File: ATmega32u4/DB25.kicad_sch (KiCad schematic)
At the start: 3 parts, among them J4 DB25_Male_MountingHoles

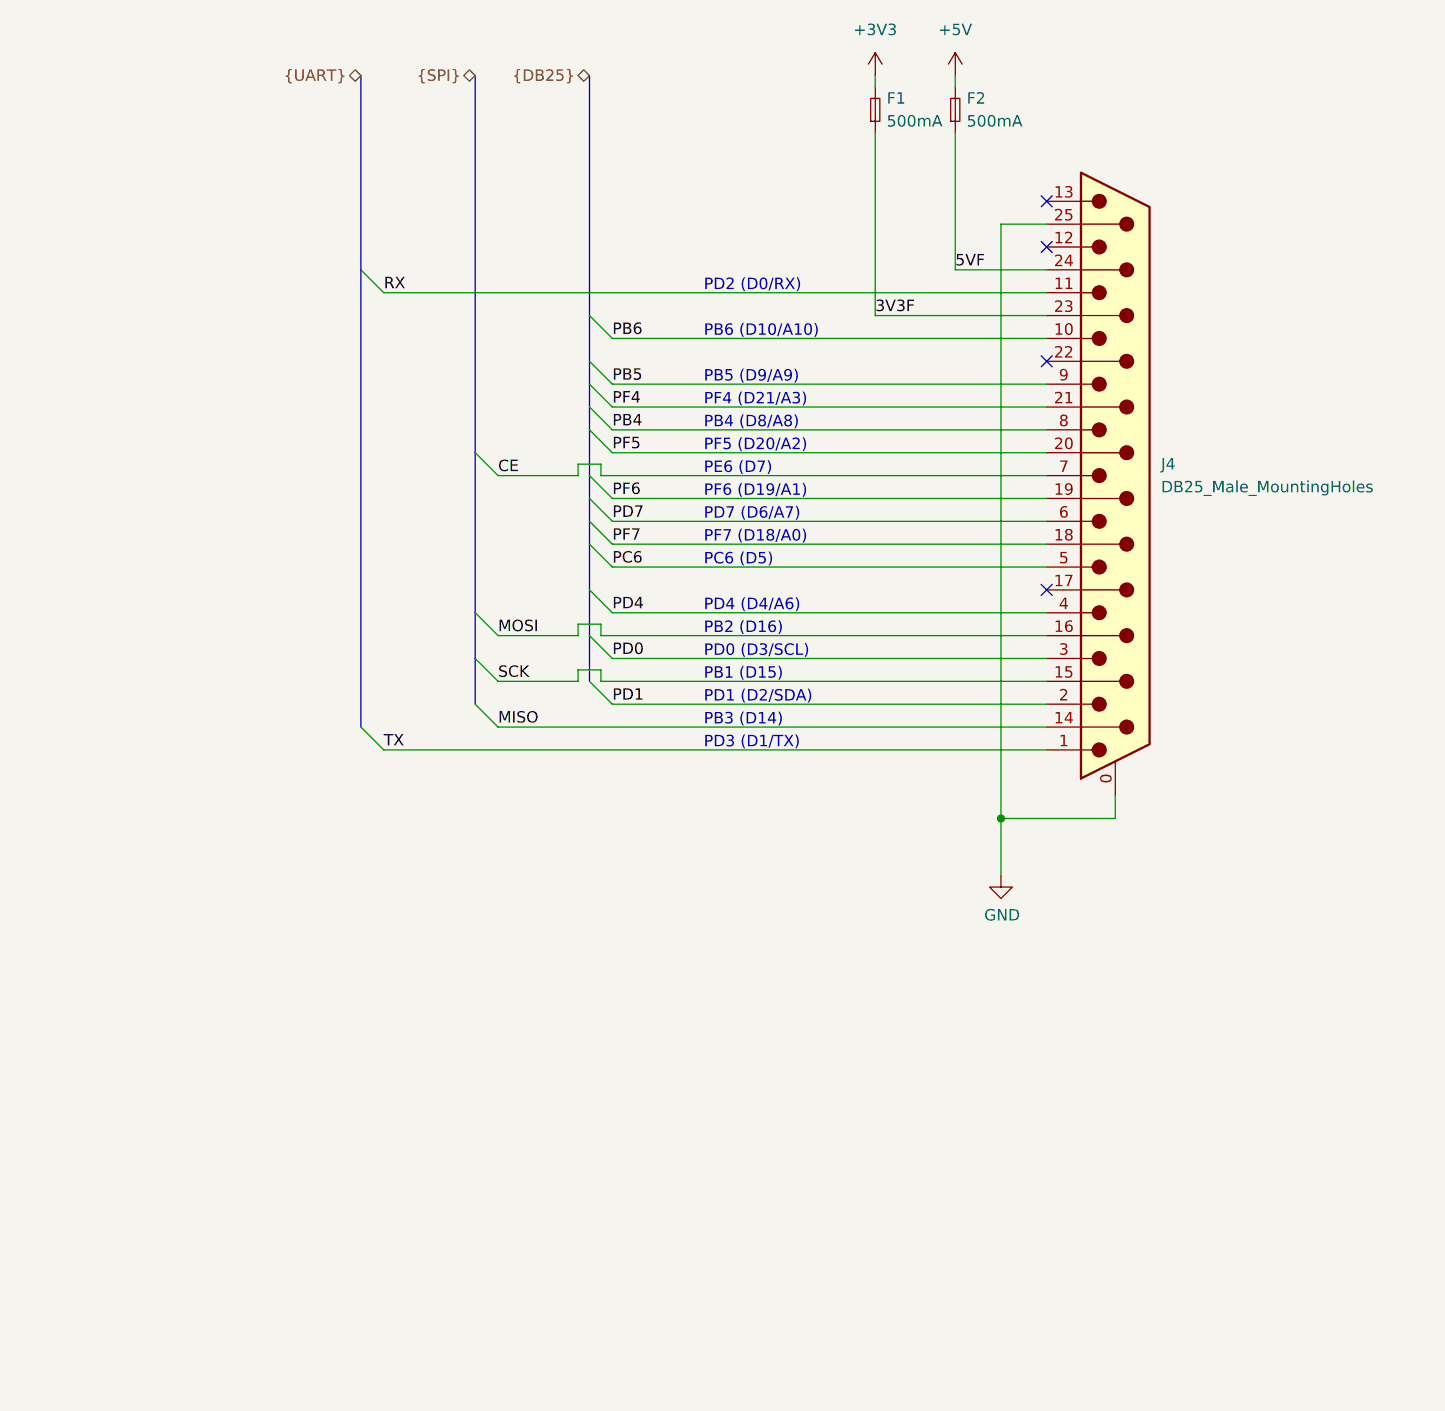
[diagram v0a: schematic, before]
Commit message: Schematic, routing and layout changes post review.
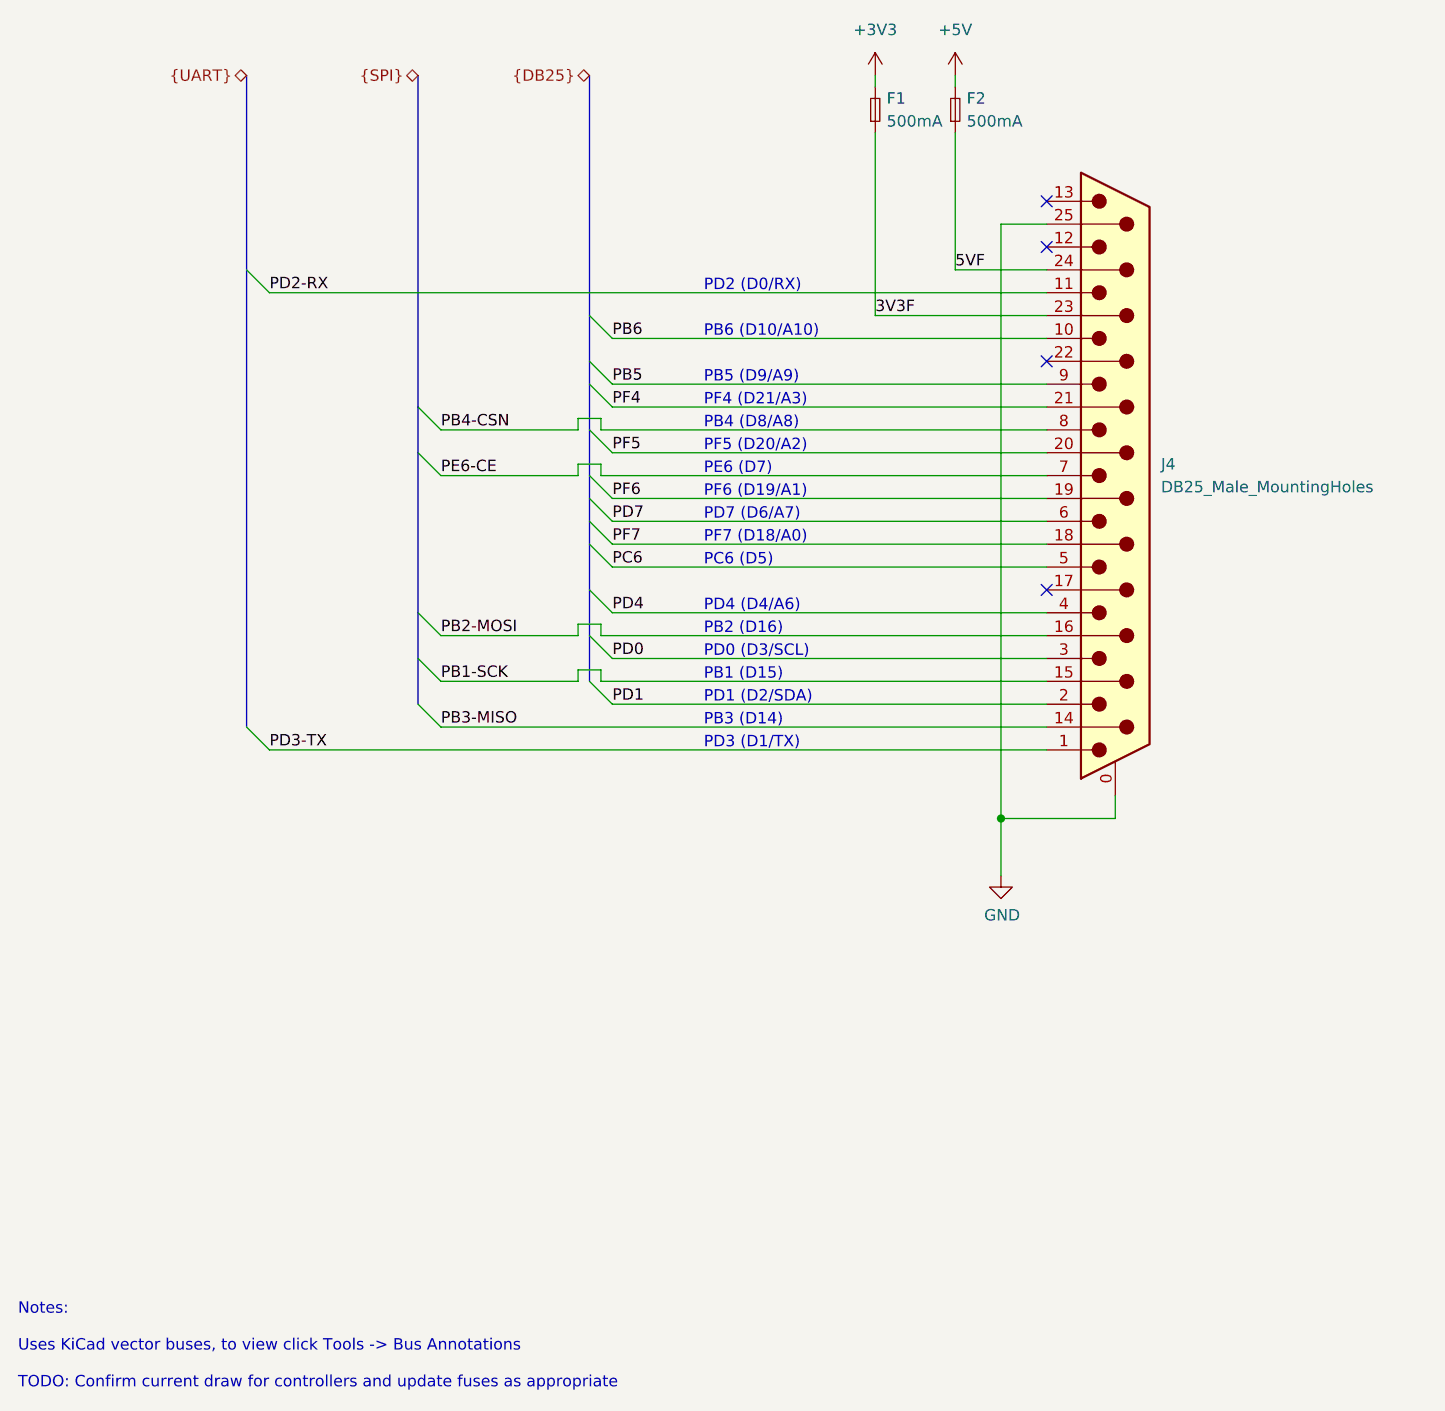
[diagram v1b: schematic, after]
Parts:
- J4: now in the parts list
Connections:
- net CE renamed PE6-CE
- net MISO renamed PB3-MISO
- net MOSI renamed PB2-MOSI
- net PB4 renamed PB4-CSN
- net RX renamed PD2-RX
- net SCK renamed PB1-SCK
- net TX renamed PD3-TX
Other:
- note added: "Notes: Uses KiCad vector buses, to view click Tools -> Bus Annotations TODO: Confirm current draw for controllers and update fuses as appropriate"
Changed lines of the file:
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@@
   (no_connect (at 127 82.55))
   (no_connect (at 127 64.77))
-  (bus_entry (at 63.5 115.57) (size 2.54 2.54)
+  (bus_entry (at 57.15 115.57) (size 2.54 2.54)
     (stroke (width 0) (type default) (color 0 0 0 0))
   )
@@
     (stroke (width 0) (type default) (color 0 0 0 0))
   )
-  (bus_entry (at 63.5 120.65) (size 2.54 2.54)
+  (bus_entry (at 57.15 120.65) (size 2.54 2.54)
     (stroke (width 0) (type default) (color 0 0 0 0))
   )
@@
     (stroke (width 0) (type default) (color 0 0 0 0))
   )
+  (bus_entry (at 57.15 87.63) (size 2.54 2.54)
+    (stroke (width 0) (type default) (color 0 0 0 0))
+  )
   (bus_entry (at 76.2 85.09) (size 2.54 2.54)
     (stroke (width 0) (type default) (color 0 0 0 0))
@@
     (stroke (width 0) (type default) (color 0 0 0 0))
   )
-  (bus_entry (at 63.5 110.49) (size 2.54 2.54)
-    (stroke (width 0) (type default) (color 0 0 0 0))
-  )
-  (bus_entry (at 76.2 87.63) (size 2.54 2.54)
+  (bus_entry (at 57.15 110.49) (size 2.54 2.54)
     (stroke (width 0) (type default) (color 0 0 0 0))
   )
@@
     (stroke (width 0) (type default) (color 0 0 0 0))
   )
-  (bus_entry (at 50.8 72.39) (size 2.54 2.54)
-    (stroke (width 0) (type default) (color 0 0 0 0))
-  )
-  (bus_entry (at 63.5 92.71) (size 2.54 2.54)
+  (bus_entry (at 38.1 72.39) (size 2.54 2.54)
+    (stroke (width 0) (type default) (color 0 0 0 0))
+  )
+  (bus_entry (at 57.15 92.71) (size 2.54 2.54)
     (stroke (width 0) (type default) (color 0 0 0 0))
   )
@@
     (stroke (width 0) (type default) (color 0 0 0 0))
   )
-  (bus_entry (at 50.8 123.19) (size 2.54 2.54)
+  (bus_entry (at 38.1 123.19) (size 2.54 2.54)
     (stroke (width 0) (type default) (color 0 0 0 0))
   )
@@
     (stroke (width 0) (type default) (color 0 0 0 0))
   )
-  (bus (pts (xy 63.5 92.71) (xy 63.5 110.49))
+  (bus (pts (xy 57.15 92.71) (xy 57.15 110.49))
     (stroke (width 0) (type default) (color 0 0 0 0))
   )
@@
     (stroke (width 0) (type default) (color 0 0 0 0))
   )
-  (wire (pts (xy 66.04 118.11) (xy 74.93 118.11))
+  (wire (pts (xy 59.69 118.11) (xy 74.93 118.11))
     (stroke (width 0) (type default) (color 0 0 0 0))
   )
@@
     (stroke (width 0) (type default) (color 0 0 0 0))
   )
-  (wire (pts (xy 66.04 113.03) (xy 74.93 113.03))
+  (wire (pts (xy 59.69 113.03) (xy 74.93 113.03))
     (stroke (width 0) (type default) (color 0 0 0 0))
   )
@@
     (stroke (width 0) (type default) (color 0 0 0 0))
   )
-  (wire (pts (xy 53.34 74.93) (xy 127 74.93))
+  (wire (pts (xy 40.64 74.93) (xy 127 74.93))
     (stroke (width 0) (type default) (color 0 0 0 0))
   )
@@
     (stroke (width 0) (type default) (color 0 0 0 0))
   )
-  (bus (pts (xy 76.2 85.09) (xy 76.2 87.63))
+  (wire (pts (xy 77.47 88.9) (xy 74.93 88.9))
+    (stroke (width 0) (type default) (color 0 0 0 0))
+  )
+  (bus (pts (xy 76.2 85.09) (xy 76.2 90.17))
     (stroke (width 0) (type default) (color 0 0 0 0))
   )
@@
     (stroke (width 0) (type default) (color 0 0 0 0))
   )
-  (bus (pts (xy 63.5 115.57) (xy 63.5 120.65))
+  (bus (pts (xy 57.15 115.57) (xy 57.15 120.65))
     (stroke (width 0) (type default) (color 0 0 0 0))
   )
@@
     (stroke (width 0) (type default) (color 0 0 0 0))
   )
-  (bus (pts (xy 50.8 50.8) (xy 50.8 72.39))
+  (bus (pts (xy 38.1 50.8) (xy 38.1 72.39))
     (stroke (width 0) (type default) (color 0 0 0 0))
   )
@@
     (stroke (width 0) (type default) (color 0 0 0 0))
   )
+  (bus (pts (xy 57.15 87.63) (xy 57.15 92.71))
+    (stroke (width 0) (type default) (color 0 0 0 0))
+  )
   (wire (pts (xy 78.74 92.71) (xy 127 92.71))
     (stroke (width 0) (type default) (color 0 0 0 0))
@@
     (stroke (width 0) (type default) (color 0 0 0 0))
   )
+  (wire (pts (xy 77.47 90.17) (xy 77.47 88.9))
+    (stroke (width 0) (type default) (color 0 0 0 0))
+  )
   (wire (pts (xy 78.74 120.65) (xy 127 120.65))
     (stroke (width 0) (type default) (color 0 0 0 0))
   )
-  (wire (pts (xy 78.74 90.17) (xy 127 90.17))
-    (stroke (width 0) (type default) (color 0 0 0 0))
-  )
-  (wire (pts (xy 53.34 125.73) (xy 127 125.73))
+  (wire (pts (xy 40.64 125.73) (xy 127 125.73))
     (stroke (width 0) (type default) (color 0 0 0 0))
   )
@@
     (stroke (width 0) (type default) (color 0 0 0 0))
   )
-  (bus (pts (xy 50.8 72.39) (xy 50.8 123.19))
+  (bus (pts (xy 38.1 72.39) (xy 38.1 123.19))
     (stroke (width 0) (type default) (color 0 0 0 0))
   )
@@
     (stroke (width 0) (type default) (color 0 0 0 0))
   )
+  (wire (pts (xy 77.47 90.17) (xy 127 90.17))
+    (stroke (width 0) (type default) (color 0 0 0 0))
+  )
   (wire (pts (xy 78.74 80.01) (xy 127 80.01))
     (stroke (width 0) (type default) (color 0 0 0 0))
@@
     (stroke (width 0) (type default) (color 0 0 0 0))
   )
-  (bus (pts (xy 63.5 110.49) (xy 63.5 115.57))
+  (wire (pts (xy 59.69 90.17) (xy 74.93 90.17))
+    (stroke (width 0) (type default) (color 0 0 0 0))
+  )
+  (wire (pts (xy 74.93 88.9) (xy 74.93 90.17))
+    (stroke (width 0) (type default) (color 0 0 0 0))
+  )
+  (bus (pts (xy 57.15 110.49) (xy 57.15 115.57))
     (stroke (width 0) (type default) (color 0 0 0 0))
   )
@@
     (stroke (width 0) (type default) (color 0 0 0 0))
   )
-  (wire (pts (xy 66.04 95.25) (xy 74.93 95.25))
+  (wire (pts (xy 59.69 95.25) (xy 74.93 95.25))
     (stroke (width 0) (type default) (color 0 0 0 0))
   )
@@
     (stroke (width 0) (type default) (color 0 0 0 0))
   )
-  (bus (pts (xy 76.2 87.63) (xy 76.2 90.17))
-    (stroke (width 0) (type default) (color 0 0 0 0))
-  )
-  (bus (pts (xy 63.5 50.8) (xy 63.5 92.71))
-    (stroke (width 0) (type default) (color 0 0 0 0))
-  )
-  (wire (pts (xy 66.04 123.19) (xy 127 123.19))
-    (stroke (width 0) (type default) (color 0 0 0 0))
+  (bus (pts (xy 57.15 50.8) (xy 57.15 87.63))
+    (stroke (width 0) (type default) (color 0 0 0 0))
+  )
+  (wire (pts (xy 59.69 123.19) (xy 127 123.19))
+    (stroke (width 0) (type default) (color 0 0 0 0))
+  )
+  (text "Notes:\n\nUses KiCad vector buses, to view click Tools -> Bus Annotations\n\nTODO: Confirm current draw for controllers and update fuses as appropriate"
+    (at 12.7 196.85 0)
+    (effects (font (size 1.27 1.27)) (justify left bottom))
   )
   (text "PD2 (D0/RX)" (at 88.9 74.93 0)
@@
     (effects (font (size 1.27 1.27)) (justify left bottom))
   )
-  (label "PB4" (at 78.74 90.17 0)
-    (effects (font (size 1.27 1.27)) (justify left bottom))
-  )
   (label "PB5" (at 78.74 85.09 0)
     (effects (font (size 1.27 1.27)) (justify left bottom))
   )
-  (label "MOSI" (at 66.04 113.03 0)
+  (label "PB2-MOSI" (at 59.69 113.03 0)
     (effects (font (size 1.27 1.27)) (justify left bottom))
   )
@@
     (effects (font (size 1.27 1.27)) (justify left bottom))
   )
-  (label "MISO" (at 66.04 123.19 0)
-    (effects (font (size 1.27 1.27)) (justify left bottom))
-  )
-  (label "TX" (at 53.34 125.73 0)
+  (label "PB3-MISO" (at 59.69 123.19 0)
+    (effects (font (size 1.27 1.27)) (justify left bottom))
+  )
+  (label "PD3-TX" (at 40.64 125.73 0)
     (effects (font (size 1.27 1.27)) (justify left bottom))
   )
@@
     (effects (font (size 1.27 1.27)) (justify left bottom))
   )
-  (label "RX" (at 53.34 74.93 0)
-    (effects (font (size 1.27 1.27)) (justify left bottom))
-  )
-  (label "CE" (at 66.04 95.25 0)
+  (label "PD2-RX" (at 40.64 74.93 0)
+    (effects (font (size 1.27 1.27)) (justify left bottom))
+  )
+  (label "PE6-CE" (at 59.69 95.25 0)
+    (effects (font (size 1.27 1.27)) (justify left bottom))
+  )
+  (label "PB4-CSN" (at 59.69 90.17 0)
     (effects (font (size 1.27 1.27)) (justify left bottom))
   )
@@
     (effects (font (size 1.27 1.27)) (justify left bottom))
   )
-  (label "SCK" (at 66.04 118.11 0)
-    (effects (font (size 1.27 1.27)) (justify left bottom))
-  )
-  (hierarchical_label "{SPI}" (shape bidirectional) (at 63.5 50.8 180)
+  (label "PB1-SCK" (at 59.69 118.11 0)
+    (effects (font (size 1.27 1.27)) (justify left bottom))
+  )
+  (hierarchical_label "{SPI}" (shape bidirectional) (at 57.15 50.8 180)
     (effects (font (size 1.27 1.27)) (justify right))
   )
-  (hierarchical_label "{UART}" (shape bidirectional) (at 50.8 50.8 180)
+  (hierarchical_label "{UART}" (shape bidirectional) (at 38.1 50.8 180)
     (effects (font (size 1.27 1.27)) (justify right))
   )
@@
   )
   (symbol (lib_id "Connector:DB25_Male_MountingHoles") (at 134.62 95.25 0) (unit 1)
-    (in_bom no) (on_board yes) (fields_autoplaced)
+    (in_bom yes) (on_board yes) (fields_autoplaced)
     (property "Reference" "J4" (id 0) (at 139.7 93.9799 0)
       (effects (font (size 1.27 1.27)) (justify left))

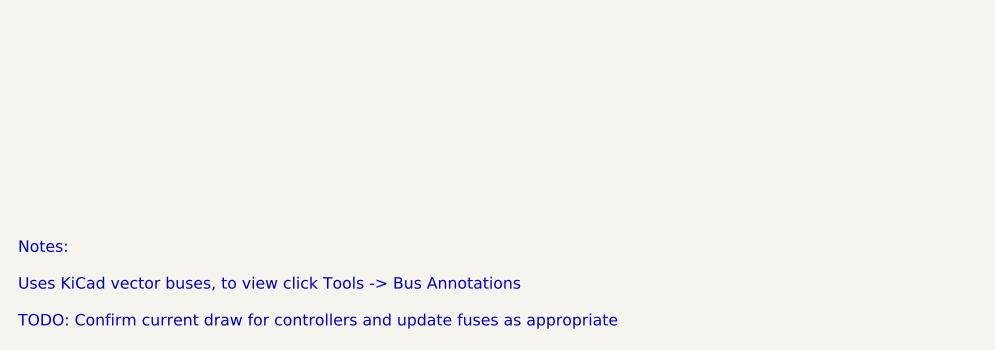
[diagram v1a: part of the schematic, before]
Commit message: Update notes, add io for reading cc pins, minor changes to schematic and routing.
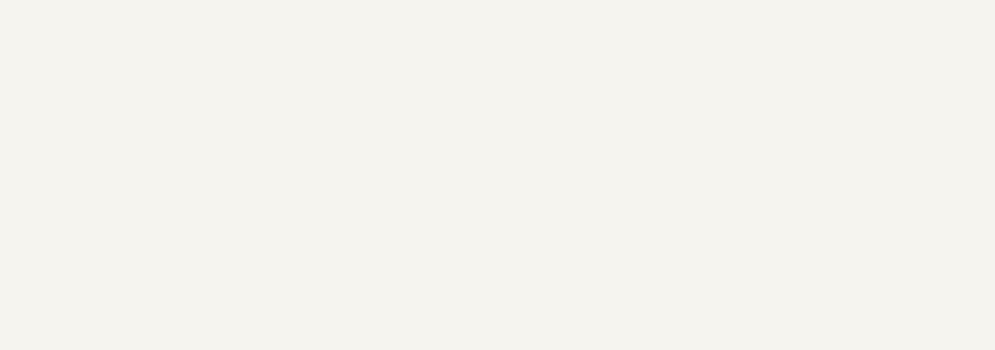
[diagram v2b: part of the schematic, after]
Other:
- note removed: "Notes: Uses KiCad vector buses, to view click Tools -> Bus Annotations TODO: Confirm current draw for controllers and update fuses as appropriate"
- title: (none) -> OpenRetroPad
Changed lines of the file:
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@@
 (kicad_sch (version 20211123) (generator eeschema)
   (paper "A4")
+  (title_block
+    (title "OpenRetroPad")
+    (date "2022-12-29")
+    (rev "2")
+    (comment 3 "github.com/OpenRetroPad")
+    (comment 4 "ATmega32u4")
+  )
   (junction (at 121.92 133.35) (diameter 0) (color 0 0 0 0)
   )
@@
     (stroke (width 0) (type default) (color 0 0 0 0))
   )
-  (text "Notes:\n\nUses KiCad vector buses, to view click Tools -> Bus Annotations\n\nTODO: Confirm current draw for controllers and update fuses as appropriate"
-    (at 12.7 196.85 0)
-    (effects (font (size 1.27 1.27)) (justify left bottom))
-  )
   (text "PD2 (D0/RX)" (at 88.9 74.93 0)
